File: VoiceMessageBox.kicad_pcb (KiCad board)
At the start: 2 copper layers, 52.2 x 37.8 mm, 6 parts, among them SW1 SW_Push, SW2 SW_Push, U1 lxb18

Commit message: Routing
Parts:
- added D1: LED, LED_THT:LED_D5.0mm, F.Cu at (73.0, 22.6)
- added H1: MountingHole, MountingHole:MountingHole_3.2mm_M3, F.Cu at (90.0, 44.2)
- added H2: MountingHole, MountingHole:MountingHole_3.2mm_M3, F.Cu at (61.5, 44.3)
- added H3: MountingHole, MountingHole:MountingHole_3.2mm_M3, F.Cu at (85.0, 31.0)
- added H4: MountingHole, MountingHole:MountingHole_3.2mm_M3, F.Cu at (72.0, 31.0)
- added R1: R, Resistor_THT:R_Axial_DIN0207_L6.3mm_D2.5mm_P10.16mm_Horizontal, F.Cu at (75.9, 32.8)
- added SW3: POWER, Button_Switch_SMD:SW_SPDT_CK-JS102011SAQN, B.Cu at (87.2, 19.8)
- BT1: footprint Battery:BatteryHolder_Keystone_2479_3xAAA -> Connector_JST:JST_EH_S2B-EH_1x02_P2.50mm_Horizontal
- LS1: moved to B.Cu
- moved LS1 87.4 mm to (66.0, 41.0), turned to 180 degrees
- moved MK1 76.8 mm to (74.0, 36.0)
- moved BT1 23.9 mm to (80.0, 41.1), turned to -90 degrees
- moved SW2 9.36 mm to (60.5, 29.0)
- moved SW1 8.66 mm to (60.5, 20.3)
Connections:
- SW1 pad 1: GND -> Net-(D1-Pad2)
- U1 pad 1: Net-(BT1-Pad1) -> Net-(U1-Pad1)
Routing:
- net Net-(LS1-Pad1): track 0.00 -> 40.6 mm
- net Net-(LS1-Pad2): track 0.00 -> 36.4 mm
- net Net-(SW2-Pad2): track 0.00 -> 23.6 mm
- net Net-(BT1-Pad1): track 0.00 -> 21.6 mm
- net Net-(U1-Pad3): track 0.00 -> 20.8 mm
- net GND: track 0.00 -> 11.6 mm
- net Net-(D1-Pad2): track 0.00 -> 11.4 mm
- net Net-(U1-Pad1): track 0.00 -> 6.77 mm
- net Net-(MK1-Pad2): track 0.00 -> 6.76 mm
- net Net-(MK1-Pad1): track 0.00 -> 5.97 mm
- net Net-(R1-Pad2): track 0.00 -> 2.92 mm
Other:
- board size 52.2 x 37.8 mm -> 35.6 x 30.3 mm

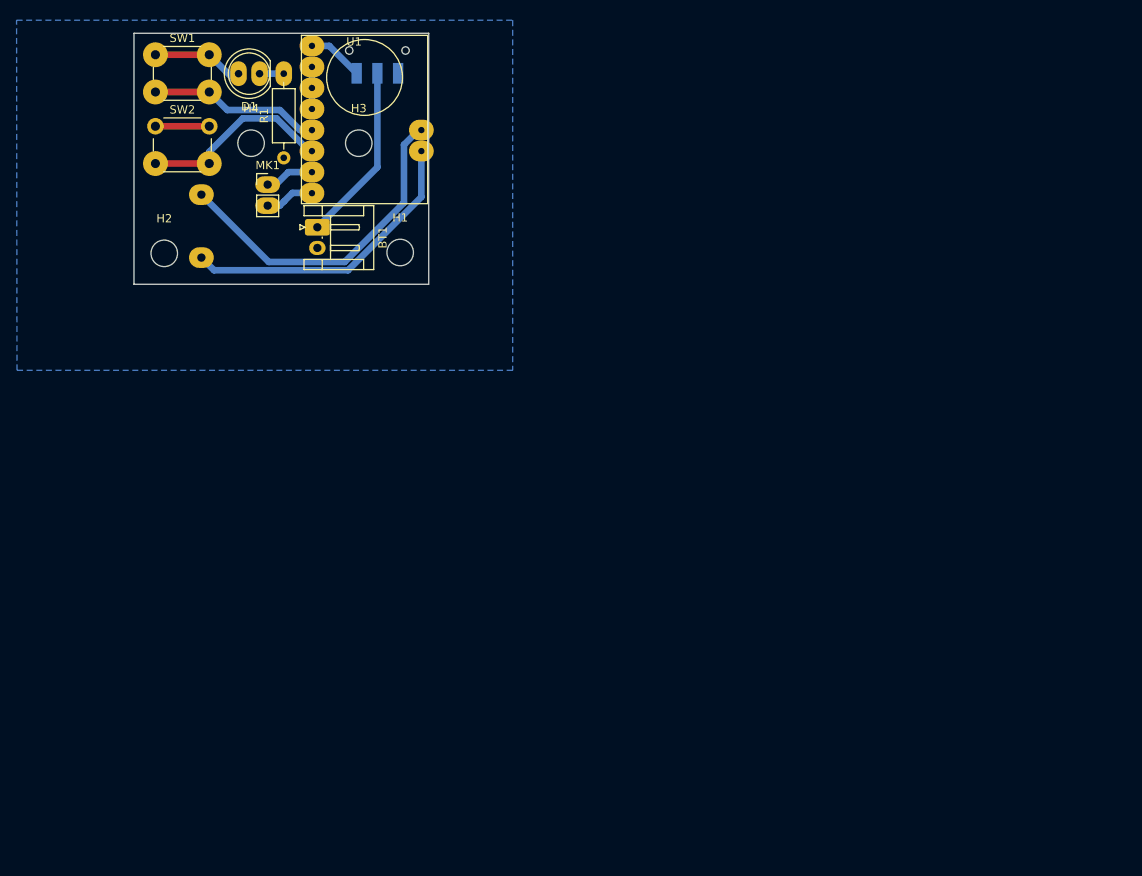
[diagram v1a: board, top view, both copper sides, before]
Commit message: Change holes for drill job
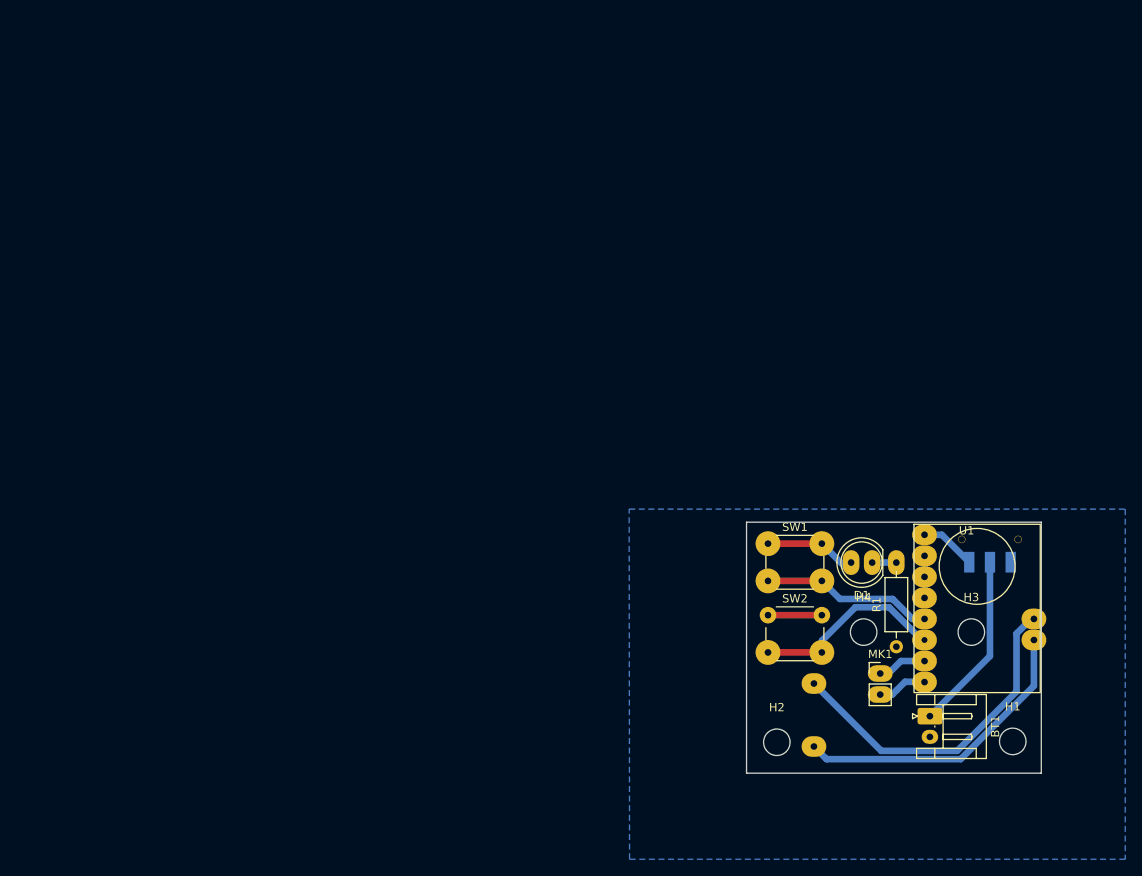
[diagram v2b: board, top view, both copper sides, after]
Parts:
- moved BT1 94.6 mm to (154.0, 100.2)
- moved D1 94.6 mm to (147.0, 81.6)
- moved H1 94.6 mm to (164.0, 103.2)
- moved H2 94.6 mm to (135.5, 103.3)
- moved H3 94.6 mm to (159.0, 90.0)
- moved H4 94.6 mm to (146.0, 90.0)
- moved LS1 94.6 mm to (140.0, 100.0)
- moved MK1 94.6 mm to (148.0, 95.0)
- moved R1 94.6 mm to (149.9, 91.8)
- moved SW1 94.6 mm to (134.4, 79.3)
- moved SW2 94.6 mm to (134.4, 88.0)
- moved SW3 94.6 mm to (161.2, 78.8)
- moved U1 94.6 mm to (158.4, 78.3)
